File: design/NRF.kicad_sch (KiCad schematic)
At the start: 18 parts, among them J2 Conn_Coaxial, U4 nRF24L01P, X2 16MHz

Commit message: Pequeños cambios
Pequeños cambios en esquemático
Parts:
- renumbered C36 to C34, C34 to C35, C35 to C36, R42 to R16
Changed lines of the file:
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@@
 		(dnp no)
 		(fields_autoplaced yes)
-		(property "Reference" "C34"
+		(property "Reference" "C35"
 			(at 177.7936 102.87 90)
 			(effects
@@
 			(project "ESCX"
 				(path "/6389d757-a1bd-4c0a-9d55-6114b19cc67a/00000000-0000-0000-0000-00005ae4952f"
-					(reference "C34")
+					(reference "C35")
 					(unit 1)
 				)
@@
 		(dnp no)
 		(fields_autoplaced yes)
-		(property "Reference" "C36"
+		(property "Reference" "C34"
 			(at 175.26 64.7762 0)
 			(effects
@@
 			(project "ESCX"
 				(path "/6389d757-a1bd-4c0a-9d55-6114b19cc67a/00000000-0000-0000-0000-00005ae4952f"
-					(reference "C36")
+					(reference "C34")
 					(unit 1)
 				)
@@
 		(dnp no)
 		(fields_autoplaced yes)
-		(property "Reference" "C35"
+		(property "Reference" "C36"
 			(at 179.0636 118.11 90)
 			(effects
@@
 			(project "ESCX"
 				(path "/6389d757-a1bd-4c0a-9d55-6114b19cc67a/00000000-0000-0000-0000-00005ae4952f"
-					(reference "C35")
+					(reference "C36")
 					(unit 1)
 				)
@@
 		(dnp no)
 		(fields_autoplaced yes)
-		(property "Reference" "R42"
+		(property "Reference" "R16"
 			(at 173.99 115.5699 0)
 			(effects
@@
 			(project "ESCX"
 				(path "/6389d757-a1bd-4c0a-9d55-6114b19cc67a/00000000-0000-0000-0000-00005ae4952f"
-					(reference "R42")
+					(reference "R16")
 					(unit 1)
 				)

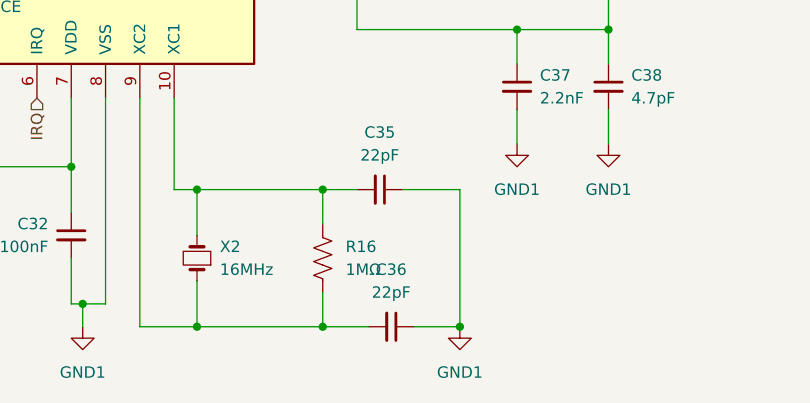
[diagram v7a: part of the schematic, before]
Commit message: Continue rooteo del MCU y modulo BT
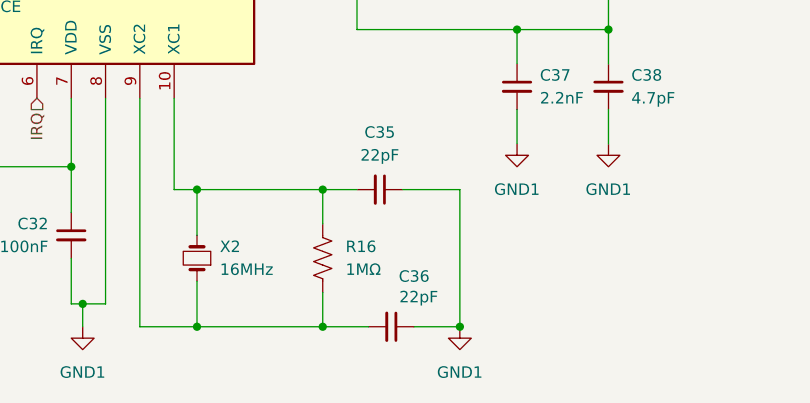
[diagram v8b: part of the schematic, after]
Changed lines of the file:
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@@
 		(on_board yes)
 		(dnp no)
-		(fields_autoplaced yes)
 		(property "Reference" "C36"
-			(at 179.0636 118.11 90)
+			(at 181.61 118.872 90)
 			(effects
 				(font
@@
 		)
 		(property "Value" "22pF"
-			(at 179.0636 120.65 90)
+			(at 182.118 121.158 90)
 			(effects
 				(font
